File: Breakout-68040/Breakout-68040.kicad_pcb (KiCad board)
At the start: 2 copper layers, 100 x 100 mm, 10 parts, among them J1 Conn_02x32_Odd_Even, J2 Conn_01x04_Pin, J3 Conn_01x32_Pin, J4 Conn_02x32_Odd_Even, J5 Conn_02x16_Odd_Even, U1 MC680LC40

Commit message: First commit
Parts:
- removed J2: Conn_01x04_Pin, Connector_PinHeader_1.27mm:PinHeader_1x04_P1.27mm_Vertical
- removed R1, R2, R3, R4: 1K, Resistor_THT:R_Axial_DIN0207_L6.3mm_D2.5mm_P10.16mm_Horizontal
- added C1: 100uF, Capacitor_SMD:C_0603_1608Metric_Pad1.08x0.95mm_HandSolder, F.Cu at (63.5, 103.4)
- added C10: 100uF, Capacitor_SMD:C_0603_1608Metric_Pad1.08x0.95mm_HandSolder, F.Cu at (45.7, 65.0)
- added C11: 100uF, Capacitor_SMD:C_0603_1608Metric_Pad1.08x0.95mm_HandSolder, F.Cu at (77.6, 64.9)
- added C12: 100uF, Capacitor_SMD:C_0603_1608Metric_Pad1.08x0.95mm_HandSolder, F.Cu at (44.6, 82.2)
- added C13: 100uF, Capacitor_SMD:C_0603_1608Metric_Pad1.08x0.95mm_HandSolder, F.Cu at (72.5, 84.6)
- added C14: 100uF, Capacitor_SMD:C_0603_1608Metric_Pad1.08x0.95mm_HandSolder, F.Cu at (99.7, 119.7)
- added C15: 100uF, Capacitor_SMD:C_0603_1608Metric_Pad1.08x0.95mm_HandSolder, F.Cu at (39.2, 114.5)
- added C16: 100uF, Capacitor_SMD:C_0603_1608Metric_Pad1.08x0.95mm_HandSolder, F.Cu at (56.0, 114.1)
- added C2: 100uF, Capacitor_SMD:C_0603_1608Metric_Pad1.08x0.95mm_HandSolder, F.Cu at (44.7, 94.7)
- added C20: 100uF, Capacitor_SMD:C_0603_1608Metric_Pad1.08x0.95mm_HandSolder, F.Cu at (72.4, 102.5)
- added C21: 100uF, Capacitor_SMD:C_0603_1608Metric_Pad1.08x0.95mm_HandSolder, F.Cu at (72.5, 94.4)
- added C22: 100uF, Capacitor_SMD:C_0603_1608Metric_Pad1.08x0.95mm_HandSolder, F.Cu at (48.4, 124.5)
- added C23: 100uF, Capacitor_SMD:C_0603_1608Metric_Pad1.08x0.95mm_HandSolder, F.Cu at (55.9, 75.8)
- added C24: 100uF, Capacitor_SMD:C_0603_1608Metric_Pad1.08x0.95mm_HandSolder, F.Cu at (45.9, 103.0)
- added C29: 100uF, Capacitor_SMD:C_0603_1608Metric_Pad1.08x0.95mm_HandSolder, F.Cu at (76.3, 114.4)
- added C3: 100uF, Capacitor_SMD:C_0603_1608Metric_Pad1.08x0.95mm_HandSolder, F.Cu at (72.5, 89.6)
- added C30: 100uF, Capacitor_SMD:C_0603_1608Metric_Pad1.08x0.95mm_HandSolder, F.Cu at (57.2, 103.1)
- added C4: 100uF, Capacitor_SMD:C_0603_1608Metric_Pad1.08x0.95mm_HandSolder, F.Cu at (44.6, 89.4)
- added C5: 100uF, Capacitor_SMD:C_0603_1608Metric_Pad1.08x0.95mm_HandSolder, F.Cu at (70.7, 75.9)
- added C6: 100uF, Capacitor_SMD:C_0603_1608Metric_Pad1.08x0.95mm_HandSolder, F.Cu at (66.2, 75.9)
- added C7: 100uF, Capacitor_SMD:C_0603_1608Metric_Pad1.08x0.95mm_HandSolder, F.Cu at (61.0, 75.8)
- added C8: 100uF, Capacitor_SMD:C_0603_1608Metric_Pad1.08x0.95mm_HandSolder, F.Cu at (48.5, 75.8)
- added D10: LED, LED_SMD:LED_0603_1608Metric_Pad1.05x0.95mm_HandSolder, F.Cu at (94.0, 72.9)
- added D11: LED, LED_SMD:LED_0603_1608Metric_Pad1.05x0.95mm_HandSolder, F.Cu at (94.0, 70.3)
- added D12: LED, LED_SMD:LED_0603_1608Metric_Pad1.05x0.95mm_HandSolder, F.Cu at (94.0, 67.7)
- added D5: LED, LED_SMD:LED_0603_1608Metric_Pad1.05x0.95mm_HandSolder, F.Cu at (94.0, 85.9)
- added D6: LED, LED_SMD:LED_0603_1608Metric_Pad1.05x0.95mm_HandSolder, F.Cu at (94.0, 83.3)
- added D7: LED, LED_SMD:LED_0603_1608Metric_Pad1.05x0.95mm_HandSolder, F.Cu at (94.0, 80.7)
- added D8: LED, LED_SMD:LED_0603_1608Metric_Pad1.05x0.95mm_HandSolder, F.Cu at (94.0, 78.1)
- added D9: LED, LED_SMD:LED_0603_1608Metric_Pad1.05x0.95mm_HandSolder, F.Cu at (94.0, 75.5)
- added IC1: DS1232S+, Package_SO:SOIC-16W_7.5x10.3mm_P1.27mm, F.Cu at (99.7, 126.4)
- added IC2: ATF22V10C-7PU, Package_DIP:DIP-24_W7.62mm_LongPads, F.Cu at (51.1, 128.3)
- added J6: Conn_01x16_Pin, Connector_PinHeader_2.54mm:PinHeader_1x16_P2.54mm_Vertical, F.Cu at (87.1, 95.5)
- added J7: Conn_01x08_Pin, Connector_PinHeader_2.54mm:PinHeader_1x08_P2.54mm_Vertical, F.Cu at (85.7, 85.6)
- added J8: Conn_02x12_Odd_Even, Connector_PinHeader_2.54mm:PinHeader_2x12_P2.54mm_Vertical, F.Cu at (51.1, 134.9)
- added R10: 1K, Resistor_SMD:R_0603_1608Metric_Pad0.98x0.95mm_HandSolder, F.Cu at (102.0, 73.0)
- added R11: 1K, Resistor_SMD:R_0603_1608Metric_Pad0.98x0.95mm_HandSolder, F.Cu at (102.0, 70.4)
- added R12: 1K, Resistor_SMD:R_0603_1608Metric_Pad0.98x0.95mm_HandSolder, F.Cu at (102.0, 67.8)
- added R5: 1K, Resistor_SMD:R_0603_1608Metric_Pad0.98x0.95mm_HandSolder, F.Cu at (102.0, 86.0)
- added R6: 1K, Resistor_SMD:R_0603_1608Metric_Pad0.98x0.95mm_HandSolder, F.Cu at (102.0, 83.4)
- added R7: 1K, Resistor_SMD:R_0603_1608Metric_Pad0.98x0.95mm_HandSolder, F.Cu at (102.0, 80.8)
- added R8: 1K, Resistor_SMD:R_0603_1608Metric_Pad0.98x0.95mm_HandSolder, F.Cu at (102.0, 78.2)
- added R9: 1K, Resistor_SMD:R_0603_1608Metric_Pad0.98x0.95mm_HandSolder, F.Cu at (102.0, 75.6)
- added SW1: SW_Push, Button_Switch_THT:SW_TH_Tactile_Omron_B3F-10xx, F.Cu at (113.2, 120.2)
- added X1: SG-615, Oscillator:Oscillator_SMD_SeikoEpson_SG8002JA-4Pin_14.0x8.7mm, F.Cu at (39.2, 123.4)
- moved U1 19.2 mm to (58.6, 89.6)
- moved J5 10.1 mm to (116.4, 68.0)
- moved J4 5.95 mm to (114.1, 144.4)
- moved J1 5.80 mm to (35.3, 56.1)
- moved J3 0.82 mm to (25.1, 140.3)
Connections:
- J4 pad 43: SC0 -> PST0
- J4 pad 45: SC1 -> PST1
- J4 pad 47: ~{MI} -> PST2
- J4 pad 49: ~{BR} -> PST3
- J4 pad 51: ~{BG} -> BCLK
- J4 pad 53: ~{BB} -> PCLK
- J5 pad 11: PST1 -> SC1
- J5 pad 13: PST2 -> ~{MI}
- J5 pad 15: PST3 -> ~{BR}
- J5 pad 17: BCLK -> ~{BG}
- J5 pad 19: PCLK -> ~{BB}
- J5 pad 9: PST0 -> SC0
- U1 pad B02: unconnected-(U1B-GND_B02-PadB02) -> GND
- U1 pad B04: unconnected-(U1B-GND_B04-PadB04) -> GND
- U1 pad B05: unconnected-(U1B-VCC_B05-PadB05) -> +5V
- U1 pad B06: unconnected-(U1B-GND_B06-PadB06) -> GND
- U1 pad B08: unconnected-(U1B-GND_B08-PadB08) -> GND
- U1 pad B09: unconnected-(U1B-VCC_B09-PadB09) -> +5V
- U1 pad B10: unconnected-(U1B-GND_B10-PadB10) -> GND
- U1 pad B13: unconnected-(U1B-GND_B13-PadB13) -> GND
- U1 pad B14: unconnected-(U1B-VCC_B14-PadB14) -> +5V
- U1 pad B15: unconnected-(U1B-GND_B15-PadB15) -> GND
- U1 pad B17: unconnected-(U1B-GND_B17-PadB17) -> GND
- U1 pad C02: unconnected-(U1B-VCC_C02-PadC02) -> +5V
- U1 pad C05: unconnected-(U1B-VCC_C05-PadC05) -> +5V
- U1 pad C06: unconnected-(U1B-GND_C06-PadC06) -> GND
- U1 pad C07: unconnected-(U1B-GND_C07-PadC07) -> GND
- U1 pad C08: unconnected-(U1B-VCC_C08-PadC08) -> +5V
- U1 pad C09: unconnected-(U1B-GND_C09-PadC09) -> GND
- U1 pad C10: unconnected-(U1B-VCC_C10-PadC10) -> +5V
- U1 pad C11: unconnected-(U1B-GND_C11-PadC11) -> GND
- U1 pad C12: unconnected-(U1B-VCC_C12-PadC12) -> +5V
- U1 pad C13: unconnected-(U1B-GND_C13-PadC13) -> GND
- U1 pad C14: unconnected-(U1B-VCC_C14-PadC14) -> +5V
- U1 pad C17: unconnected-(U1B-VCC_C17-PadC17) -> +5V
- U1 pad D02: unconnected-(U1B-GND_D02-PadD02) -> GND
- U1 pad D17: unconnected-(U1B-GND_D17-PadD17) -> GND
- U1 pad F02: unconnected-(U1B-GND_F02-PadF02) -> GND
- U1 pad F17: unconnected-(U1B-GND_F17-PadF17) -> GND
- U1 pad G02: unconnected-(U1B-VCC_G02-PadG02) -> +5V
- U1 pad G17: unconnected-(U1B-VCC_G17-PadG17) -> +5V
- U1 pad H02: unconnected-(U1B-GND_H02-PadH02) -> GND
- U1 pad H03: unconnected-(U1B-VCC_H03-PadH03) -> +5V
- U1 pad H16: unconnected-(U1B-VCC_H16-PadH16) -> +5V
- U1 pad H17: unconnected-(U1B-GND_H17-PadH17) -> GND
- U1 pad J03: unconnected-(U1B-VCC_J03-PadJ03) -> +5V
- U1 pad J16: unconnected-(U1B-VCC_J16-PadJ16) -> +5V
- U1 pad K03: unconnected-(U1B-GND_K03-PadK03) -> GND
- U1 pad K16: unconnected-(U1B-GND_K16-PadK16) -> GND
- U1 pad L02: unconnected-(U1B-GND_L02-PadL02) -> GND
- U1 pad L03: unconnected-(U1B-GND_L03-PadL03) -> GND
- U1 pad L16: unconnected-(U1B-VCC_L16-PadL16) -> +5V
- U1 pad L17: unconnected-(U1B-GND_L17-PadL17) -> GND
- U1 pad M02: unconnected-(U1B-VCC_M02-PadM02) -> +5V
- U1 pad M03: unconnected-(U1B-VCC_M03-PadM03) -> +5V
- U1 pad M16: unconnected-(U1B-GND_M16-PadM16) -> GND
- U1 pad M17: unconnected-(U1B-VCC_M17-PadM17) -> +5V
- U1 pad N02: unconnected-(U1B-GND_N02-PadN02) -> GND
- U1 pad N17: unconnected-(U1B-GND_N17-PadN17) -> GND
- U1 pad Q02: unconnected-(U1B-GND_Q02-PadQ02) -> GND
- U1 pad Q17: unconnected-(U1B-GND_Q17-PadQ17) -> GND
- U1 pad R02: unconnected-(U1B-VCC_R02-PadR02) -> +5V
- U1 pad R04: unconnected-(U1B-GND_R04-PadR04) -> GND
- U1 pad R05: unconnected-(U1B-VCC_R05-PadR05) -> +5V
- U1 pad R06: unconnected-(U1B-GND_R06-PadR06) -> GND
- U1 pad R08: unconnected-(U1B-VCC_R08-PadR08) -> +5V
- U1 pad R10: unconnected-(U1B-GND_R10-PadR10) -> GND
- U1 pad R11: unconnected-(U1B-GND_R11-PadR11) -> GND
- U1 pad R12: unconnected-(U1B-VCC_R12-PadR12) -> +5V
- U1 pad R13: unconnected-(U1B-GND_R13-PadR13) -> GND
- U1 pad R17: unconnected-(U1B-VCC_R17-PadR17) -> +5V
- U1 pad S02: unconnected-(U1B-GND_S02-PadS02) -> GND
- U1 pad S08: unconnected-(U1B-VCC_S08-PadS08) -> +5V
- U1 pad S09: unconnected-(U1B-GND_S09-PadS09) -> GND
- U1 pad S10: unconnected-(U1B-GND_S10-PadS10) -> GND
- U1 pad S15: unconnected-(U1B-GND_S15-PadS15) -> GND
- U1 pad S16: unconnected-(U1B-VCC_S16-PadS16) -> +5V
- U1 pad S17: unconnected-(U1B-GND_S17-PadS17) -> GND
- U1 pad T04: unconnected-(U1B-GND_T04-PadT04) -> GND
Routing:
- net GND: track 0.00 -> 81.5 mm, vias 0 -> 34
- net +5V: track 0.00 -> 52.5 mm, vias 0 -> 25
- net PCLK: track 0.00 -> 35.9 mm
- net BCLK: track 0.00 -> 15.8 mm
- net Net-(D5-A): track 0.00 -> 7.54 mm
- net Net-(D6-A): track 0.00 -> 7.52 mm
- net Net-(D7-A): track 0.00 -> 7.50 mm
- net Net-(D8-A): track 0.00 -> 7.47 mm
- net Net-(D12-A): track 0.00 -> 7.46 mm
- net Net-(D9-A): track 0.00 -> 7.45 mm
- net Net-(D11-A): track 0.00 -> 7.44 mm
- net Net-(D10-A): track 0.00 -> 7.43 mm
- net Net-(D5-K): track 0.00 -> 6.27 mm
- net Net-(D6-K): track 0.00 -> 6.27 mm
- net Net-(D7-K): track 0.00 -> 6.27 mm
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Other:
- copper layers 2 -> 4
- board text removed: "GND"

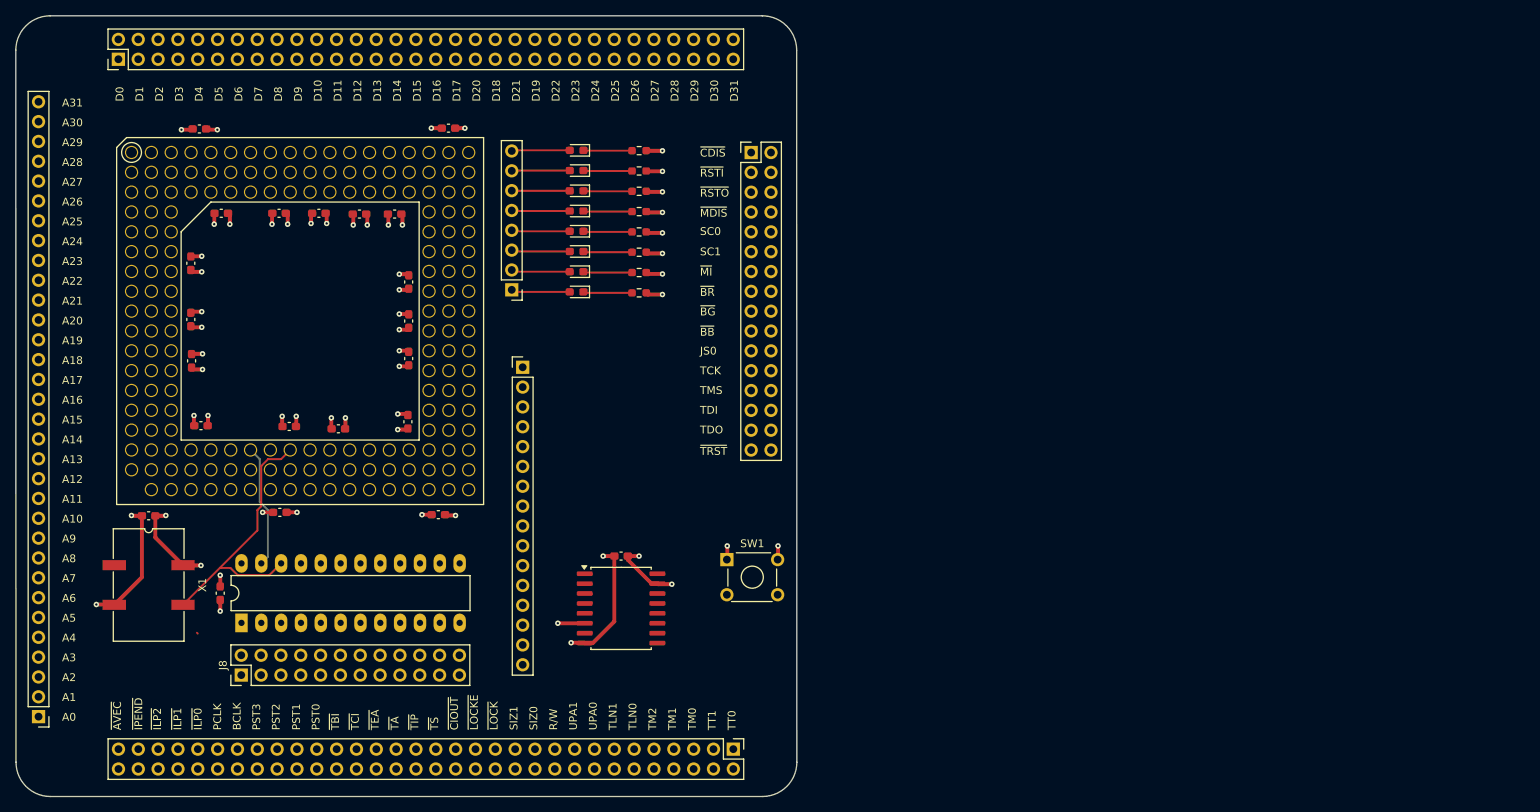
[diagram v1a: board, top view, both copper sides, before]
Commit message: First routed version
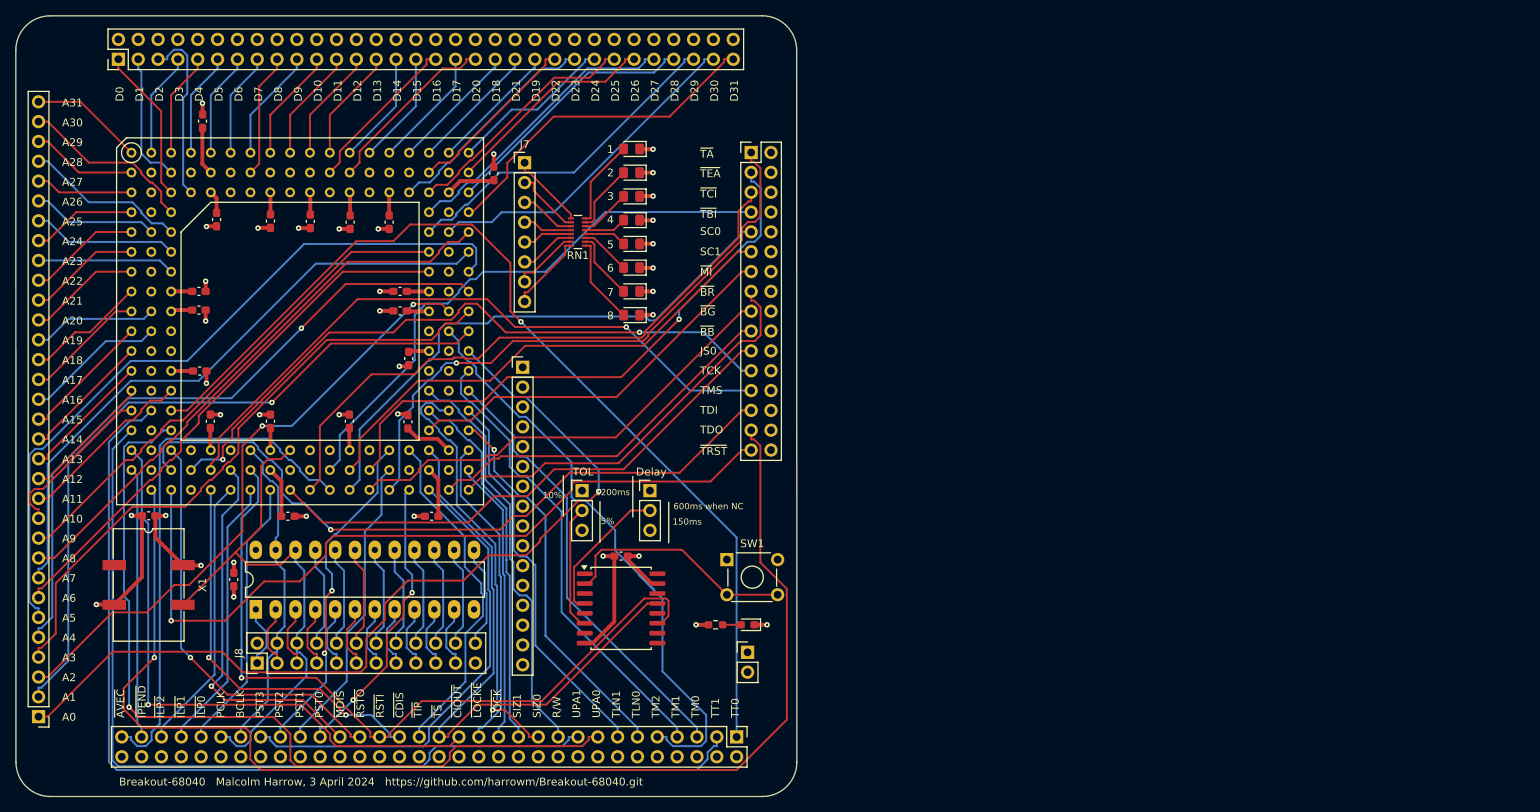
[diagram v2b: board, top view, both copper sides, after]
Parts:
- removed C16, C24, C30: 100uF, Capacitor_SMD:C_0603_1608Metric_Pad1.08x0.95mm_HandSolder
- removed D10, D11, D12, D5, D6, D7, D8, D9: LED, LED_SMD:LED_0603_1608Metric_Pad1.05x0.95mm_HandSolder
- removed R10, R11, R12, R5, R6, R7, R8, R9: 1K, Resistor_SMD:R_0603_1608Metric_Pad0.98x0.95mm_HandSolder
- added C17: 100uF, Capacitor_SMD:C_0603_1608Metric_Pad1.08x0.95mm_HandSolder, F.Cu at (57.0, 114.6)
- added C18: 100uF, Capacitor_SMD:C_0603_1608Metric_Pad1.08x0.95mm_HandSolder, F.Cu at (47.1, 102.4)
- added C19: 100uF, Capacitor_SMD:C_0603_1608Metric_Pad1.08x0.95mm_HandSolder, F.Cu at (54.8, 102.4)
- added D1: Power LED, LED_SMD:LED_0603_1608Metric_Pad1.05x0.95mm_HandSolder, F.Cu at (115.9, 128.5)
- added D19: LED, LED_SMD:LED_0805_2012Metric_Pad1.15x1.40mm_HandSolder, F.Cu at (101.0, 67.6)
- added D20: LED, LED_SMD:LED_0805_2012Metric_Pad1.15x1.40mm_HandSolder, F.Cu at (101.0, 70.6)
- added D21: LED, LED_SMD:LED_0805_2012Metric_Pad1.15x1.40mm_HandSolder, F.Cu at (101.0, 73.6)
- added D22: LED, LED_SMD:LED_0805_2012Metric_Pad1.15x1.40mm_HandSolder, F.Cu at (101.0, 76.7)
- added D23: LED, LED_SMD:LED_0805_2012Metric_Pad1.15x1.40mm_HandSolder, F.Cu at (101.0, 79.7)
- added D24: LED, LED_SMD:LED_0805_2012Metric_Pad1.15x1.40mm_HandSolder, F.Cu at (101.0, 82.8)
- added D25: LED, LED_SMD:LED_0805_2012Metric_Pad1.15x1.40mm_HandSolder, F.Cu at (101.0, 85.8)
- added D26: LED, LED_SMD:LED_0805_2012Metric_Pad1.15x1.40mm_HandSolder, F.Cu at (101.0, 88.8)
- added J10: Conn_01x03_Pin, Connector_PinHeader_2.54mm:PinHeader_1x03_P2.54mm_Vertical, F.Cu at (94.7, 111.3)
- added J2: Conn_01x02_Pin, Connector_PinHeader_2.54mm:PinHeader_1x02_P2.54mm_Vertical, F.Cu at (115.9, 132.0)
- added J9: Conn_01x03_Pin, Connector_PinHeader_2.54mm:PinHeader_1x03_P2.54mm_Vertical, F.Cu at (103.4, 111.3)
- added R1: 1K, Resistor_SMD:R_0603_1608Metric_Pad0.98x0.95mm_HandSolder, F.Cu at (111.8, 128.5)
- added RN1: 1K, Resistor_SMD:R_Array_Convex_8x0602, F.Cu at (94.2, 78.2)
- SW1: value SW_Push -> Reset
- moved J7 16.4 mm to (87.3, 69.3), turned to 0 degrees
- moved C11 8.20 mm to (83.4, 70.7), turned to 90 degrees
- moved C12 3.75 mm to (45.6, 85.8), turned to 0 degrees
- moved J8 2.56 mm to (53.1, 133.4)
- moved IC2 2.52 mm to (52.9, 126.5)
- moved C22 2.46 mm to (50.1, 122.7)
- moved C3 1.70 mm to (71.4, 88.3), turned to 180 degrees
- moved C1 1.70 mm to (64.9, 102.4), turned to 90 degrees
- moved C2 1.66 mm to (45.7, 96.0), turned to 0 degrees
- moved C13 1.63 mm to (71.4, 85.8), turned to 180 degrees
- moved J4 1.62 mm to (114.5, 142.9)
- moved C4 1.59 mm to (45.6, 88.2), turned to 0 degrees
- moved C6 1.59 mm to (65.0, 76.9), turned to -90 degrees
- moved C7 1.51 mm to (59.9, 76.8), turned to -90 degrees
- moved C23 1.49 mm to (54.8, 76.8), turned to -90 degrees
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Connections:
- IC1 pad 4: unconnected-(IC1-TD-Pad4) -> Net-(IC1-TD)
- IC1 pad 6: +5V -> Net-(IC1-TOL)
- J4 pad 35: ~{TA} -> ~{CDIS}
- J4 pad 37: ~{TEA} -> ~{RSTI}
- J4 pad 39: ~{TCI} -> ~{RSTO}
- J4 pad 41: ~{TBI} -> ~{MDIS}
- J5 pad 1: ~{CDIS} -> ~{TA}
- J5 pad 3: ~{RSTI} -> ~{TEA}
- J5 pad 5: ~{RSTO} -> ~{TCI}
- J5 pad 7: ~{MDIS} -> ~{TBI}
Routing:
- net TDO: track 0.00 -> 161.9 mm, vias 0 -> 1
- net TT1: track 0.00 -> 129.3 mm
- net TT0: track 0.00 -> 128.1 mm, vias 0 -> 1
- net A0: track 0.00 -> 115.1 mm, vias 0 -> 1
- net UPA0: track 0.00 -> 107.9 mm, vias 0 -> 1
- net UPA1: track 0.00 -> 105.5 mm
- net ~{TRST}: track 0.00 -> 101.5 mm, vias 0 -> 1
- net ~{RSTI}: track 0.00 -> 97.5 mm, vias 0 -> 1
- net A5: track 0.00 -> 93.6 mm
- net TDI: track 0.00 -> 91.7 mm, vias 0 -> 1
- net A1: track 0.00 -> 90.0 mm, vias 0 -> 1
- net TCK: track 0.00 -> 85.8 mm, vias 0 -> 2
- net A4: track 0.00 -> 85.7 mm, vias 0 -> 1
- net TMS: track 0.00 -> 84.9 mm, vias 0 -> 1
- net A7: track 0.00 -> 80.4 mm
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- added copper zone on In2.Cu, net +5V
- added copper zone on In1.Cu, net GND
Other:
- board text added: "+5V"
- board text added: "1"
- board text added: "10%"
- board text added: "1200ms"
- board text added: "150ms"
- board text added: "2"
- board text added: "3"
- board text added: "4"
- board text added: "5"
- board text added: "5%"
- board text added: "6"
- board text added: "600ms when NC"
- board text added: "7"
- board text added: "8"
- board text added: "Breakout-68040 Malcolm Harrow, 3 April 2024 https://github.com/harrowm/Breakout-68040.git"
- board text added: "Delay"
- board text added: "GND"
- board text added: "TOL"

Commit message: JLCPCB manufacturing info
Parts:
- added RN2: R_Pack04, Resistor_SMD:R_Array_Convex_4x0603, F.Cu at (94.3, 83.1)
- C10, C11, C12, C13, C14, C15, C17, C18, C19, C20, C21, C22, C23, C29, C4, C5, C6, C7, C8: value 100uF -> 100nF; footprint Capacitor_SMD:C_0603_1608Metric_Pad1.08x0.95mm_HandSolder -> Capacitor_SMD:C_0805_2012Metric_Pad1.18x1.45mm_HandSolder
- D1: footprint LED_SMD:LED_0603_1608Metric_Pad1.05x0.95mm_HandSolder -> LED_SMD:LED_0805_2012Metric_Pad1.15x1.40mm_HandSolder
- R1: footprint Resistor_SMD:R_0603_1608Metric_Pad0.98x0.95mm_HandSolder -> Resistor_SMD:R_0805_2012Metric_Pad1.20x1.40mm_HandSolder
- RN1: footprint Resistor_SMD:R_Array_Convex_8x0602 -> Resistor_SMD:R_Array_Convex_4x0603
- moved RN1 5.50 mm to (94.3, 72.7)
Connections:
- RN1 pad 1: Net-(D26-A) -> Net-(D22-A)
- RN1 pad 2: Net-(D25-A) -> Net-(D21-A)
- RN1 pad 3: Net-(D24-A) -> Net-(D20-A)
- RN1 pad 4: Net-(D23-A) -> Net-(D19-A)
- RN1 pad 5: Net-(D22-A) -> Net-(J7-Pin_1)
- RN1 pad 6: Net-(D21-A) -> Net-(J7-Pin_2)
- RN1 pad 7: Net-(D20-A) -> Net-(J7-Pin_3)
- RN1 pad 8: Net-(D19-A) -> Net-(J7-Pin_4)
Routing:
- net A1: track 90.0 -> 173.1 mm, vias 1 -> 0
- net TDO: track 161.9 -> 129.4 mm, vias 1 -> 2
- net PST2: track 43.4 -> 71.6 mm, vias 2 -> 0
- net A0: track 115.1 -> 88.7 mm, vias 1 -> 0
- net ~{CIOUT}: track 76.4 -> 97.4 mm, vias 1 -> 0
- net A4: track 85.7 -> 104.6 mm, vias 1 -> 0
- net TT0: track 128.1 -> 110.4 mm, vias 1 -> 0
- net ~{TA}: track 77.4 -> 94.8 mm, vias 1 -> 0
- net ~{AVEC}: track 68.1 -> 50.8 mm, vias 0 -> 2
- net TM2: track 77.5 -> 64.3 mm
- net A2: track 79.2 -> 92.1 mm, vias 2 -> 0
- net TM0: track 56.9 -> 66.7 mm
- net UPA1: track 105.5 -> 95.8 mm
- net PST3: track 61.2 -> 51.6 mm, vias 0 -> 2
- net A8: track 73.0 -> 82.4 mm
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
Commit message: Sent to jclpcb
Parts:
- C1, C2, C3: value 100uF -> 100nF; footprint Capacitor_SMD:C_0603_1608Metric_Pad1.08x0.95mm_HandSolder -> Capacitor_SMD:C_0805_2012Metric_Pad1.18x1.45mm_HandSolder
- moved C1 0.22 mm to (65.0, 102.6)
- moved C2 0.20 mm to (45.6, 95.9)
- moved C3 0.12 mm to (71.5, 88.2)
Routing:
- net ~{CIOUT}: track 97.4 -> 88.2 mm
- net +5V: track 98.4 -> 94.1 mm
- net Net-(IC1-~{PBRST}): track 30.4 -> 31.2 mm
- net ~{TS}: track 81.1 -> 80.5 mm
